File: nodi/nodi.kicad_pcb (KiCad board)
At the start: 2 copper layers, 109.7 x 90.2 mm, 19 parts, among them J1 MJ-4PP-9, SW10 SW_PUSH, SW11 SW_PUSH, SW12 SW_PUSH, SW14 SW_PUSH, SW15 SW_PUSH, SW16 SW_PUSH, SW17 SW_PUSH, SW18 SW_PUSH, SW2 SW_PUSH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

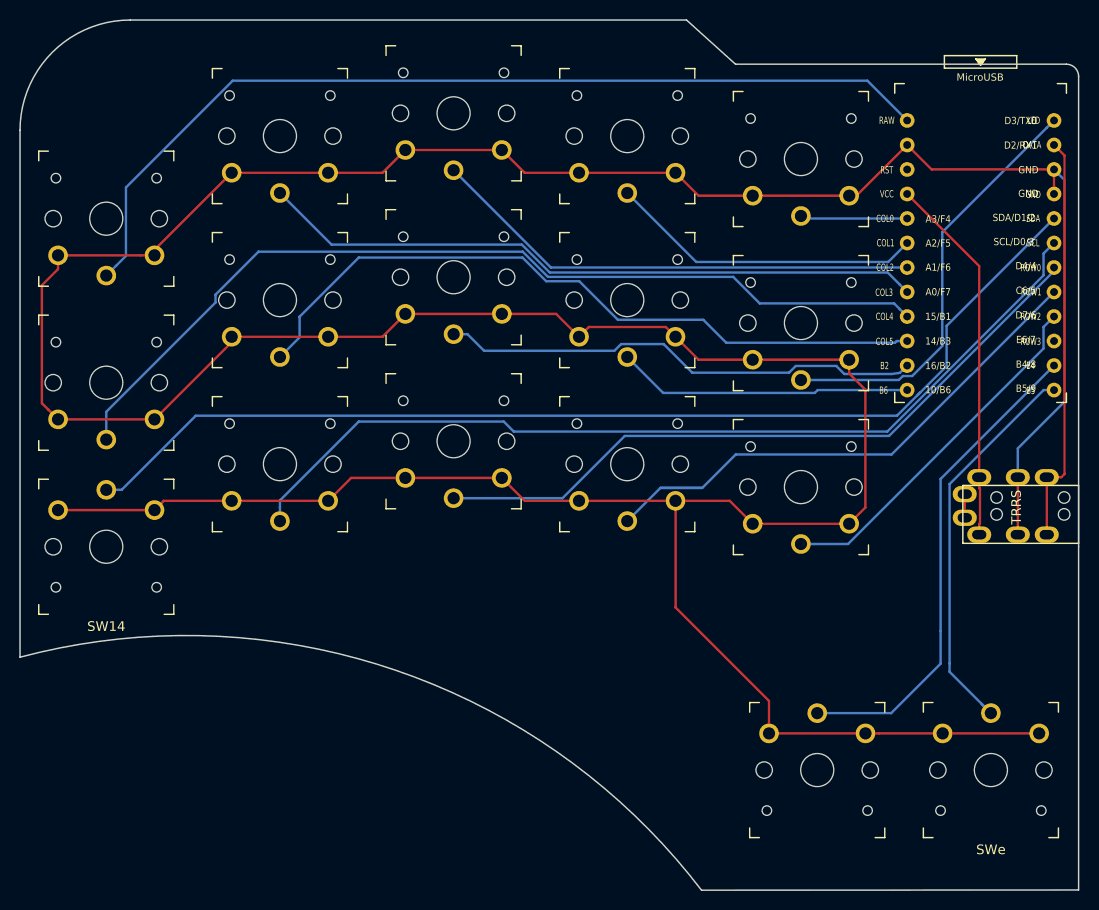
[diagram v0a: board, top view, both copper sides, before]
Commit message: Maybe don't wire q to raw?
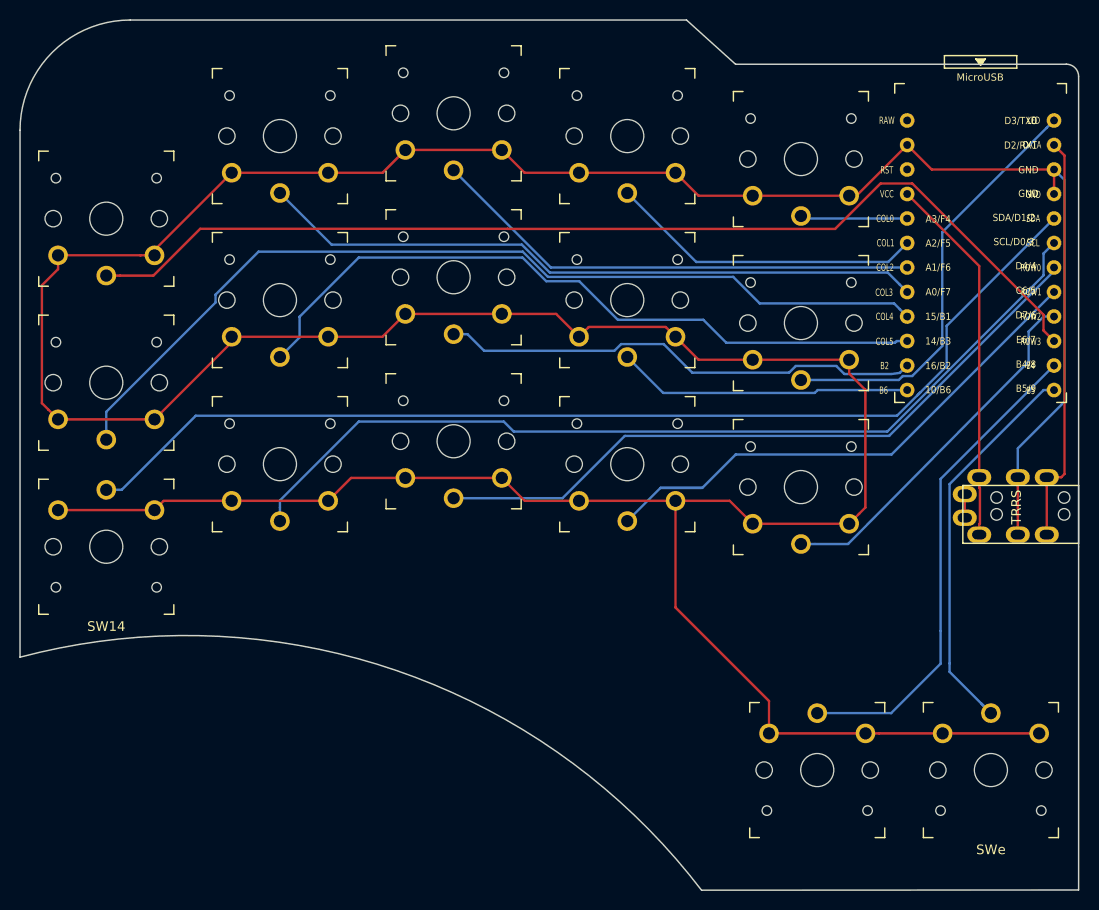
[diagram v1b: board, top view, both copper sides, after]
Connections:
- SW2 pad 1: Net-(U1-Pad24) -> row3
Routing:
- net row3: track 0.00 -> 109.9 mm
- net Net-(U1-Pad24): track 97.2 -> 0.00 mm
- net row2: track 37.3 -> 37.9 mm
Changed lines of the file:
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@@
     (thickness 1.6)
     (drawings 10)
-    (tracks 193)
+    (tracks 199)
     (zones 0)
     (modules 19)
@@
   )
   (setup
-    (last_trace_width 0.5)
+    (last_trace_width 0.25)
     (user_trace_width 0.5)
     (trace_clearance 0.2)
@@
       (net 6 GND))
     (pad 1 thru_hole circle (at 0 5.9) (size 2.032 2.032) (drill 1.27) (layers *.Cu *.Mask)
-      (net 23 "Net-(U1-Pad24)"))
+      (net 4 row3))
     (pad "" np_thru_hole circle (at 5.22 -4.2) (size 0.9906 0.9906) (drill 0.9906) (layers *.Cu *.Mask))
     (pad "" np_thru_hole circle (at 5.5 0) (size 1.7018 1.7018) (drill 1.7018) (layers *.Cu *.Mask))
@@
   (segment (start 109.240301 61.540301) (end 105.776603 65.003999) (width 0.25) (layer B.Cu) (net 2))
   (segment (start 117.43684 70.82) (end 116 70.82) (width 0.25) (layer B.Cu) (net 3))
-  (segment (start 141.144399 50.560283) (end 120.884682 70.82) (width 0.25) (layer B.Cu) (net 3))
   (segment (start 120.884682 70.82) (end 117.43684 70.82) (width 0.25) (layer B.Cu) (net 3))
-  (segment (start 141.144399 48.329001) (end 141.144399 50.560283) (width 0.25) (layer B.Cu) (net 3))
-  (segment (start 142.2314 47.242) (end 141.144399 48.329001) (width 0.25) (layer B.Cu) (net 3))
+  (segment (start 139.6 48.79577) (end 139.6 51.9) (width 0.25) (layer B.Cu) (net 3))
+  (segment (start 141.15377 47.242) (end 139.6 48.79577) (width 0.25) (layer B.Cu) (net 3))
+  (segment (start 142.2314 47.242) (end 141.15377 47.242) (width 0.25) (layer B.Cu) (net 3))
+  (segment (start 139.6 51.9) (end 120.884682 70.82) (width 0.25) (layer B.Cu) (net 3))
+  (segment (start 45.43684 43) (end 44 43) (width 0.25) (layer F.Cu) (net 4))
+  (segment (start 48.884682 43) (end 45.43684 43) (width 0.25) (layer F.Cu) (net 4))
+  (segment (start 53.734983 38.149699) (end 48.884682 43) (width 0.25) (layer F.Cu) (net 4))
+  (segment (start 85.625047 38.161001) (end 85.613745 38.149699) (width 0.25) (layer F.Cu) (net 4))
+  (segment (start 124.249683 33.454999) (end 119.543681 38.161001) (width 0.25) (layer F.Cu) (net 4))
+  (segment (start 127.533161 33.454999) (end 124.249683 33.454999) (width 0.25) (layer F.Cu) (net 4))
+  (segment (start 85.613745 38.149699) (end 53.734983 38.149699) (width 0.25) (layer F.Cu) (net 4))
+  (segment (start 119.543681 38.161001) (end 85.625047 38.161001) (width 0.25) (layer F.Cu) (net 4))
+  (segment (start 141.144399 47.066237) (end 127.533161 33.454999) (width 0.25) (layer F.Cu) (net 4))
+  (segment (start 141.144399 48.694999) (end 141.144399 47.066237) (width 0.25) (layer F.Cu) (net 4))
+  (segment (start 142.2314 49.782) (end 141.144399 48.694999) (width 0.25) (layer F.Cu) (net 4))
   (segment (start 116.262 37.082) (end 116 36.82) (width 0.25) (layer B.Cu) (net 5))
   (segment (start 127.0114 37.082) (end 116.262 37.082) (width 0.25) (layer B.Cu) (net 5))
@@
   (segment (start 130.4767 83.2233) (end 125.35 88.35) (width 0.25) (layer B.Cu) (net 21))
   (segment (start 132.98 65.65) (end 132.98 68.1) (width 0.25) (layer F.Cu) (net 22))
-  (segment (start 45.015999 41.984001) (end 44 43) (width 0.25) (layer B.Cu) (net 23))
-  (segment (start 46.039501 40.960499) (end 45.015999 41.984001) (width 0.25) (layer B.Cu) (net 23))
-  (segment (start 57.105653 22.800301) (end 46.039501 33.866453) (width 0.25) (layer B.Cu) (net 23))
-  (segment (start 46.039501 33.866453) (end 46.039501 40.960499) (width 0.25) (layer B.Cu) (net 23))
-  (segment (start 122.889701 22.800301) (end 57.105653 22.800301) (width 0.25) (layer B.Cu) (net 23))
-  (segment (start 127.0114 26.922) (end 122.889701 22.800301) (width 0.25) (layer B.Cu) (net 23))
 )
